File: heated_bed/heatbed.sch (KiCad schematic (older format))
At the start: 9 parts, among them P1 CONN_POWER, P2 CONN_2

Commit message: Feita a primeira metade da PCB, com duas trilhas de aquecimento prontas. Restam as duas trilhas com menos interferencia externa
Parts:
- removed P1: CONN_POWER, symbol CONN_2
- removed P2: CONN_2, symbol CONN_2
- added MH1, MH2, MH3, MH4: MOUNTING_HOLE, MountingHole_3mm_RevA_Date21Jun2010, symbol MOUNTING_HOLE
- added P1: CONN_4, bornier4, symbol CONN_4
- added PCB_R11, PCB_R21, PCB_R31, PCB_R41: 4R, SM1206, symbol R
- added TH2: 100k, SM0603, symbol THERMISTOR
- D1: footprint (none) -> LED-0805
- PCB_R1, PCB_R2, PCB_R3, PCB_R4: footprint (none) -> SM1206
- R1: footprint (none) -> SM0805
- TH1: footprint 0805,0603 -> SM0805
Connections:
- net labels added: Heater 1
- wire segments 16 -> 18
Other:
- moved on the sheet: PCB_R1, PCB_R2, PCB_R3, PCB_R4, R1, TH1

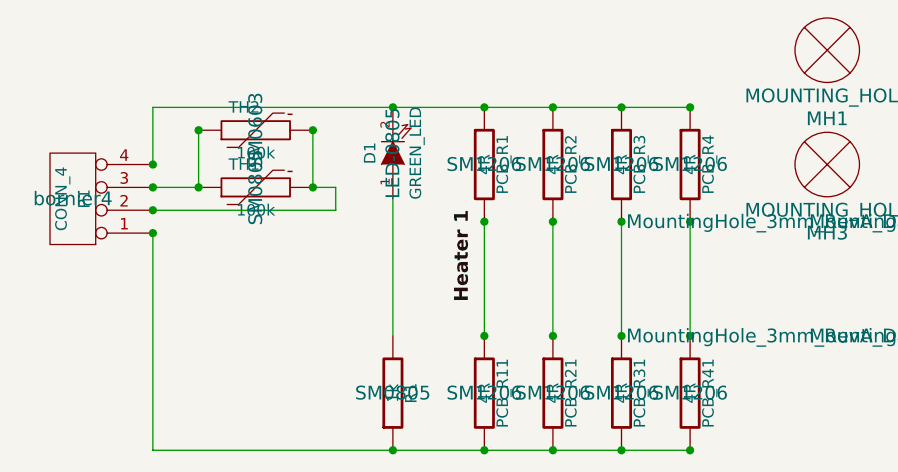
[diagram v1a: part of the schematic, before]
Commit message: Removidos resistores de PCB do esquematico para facilitar DRC.
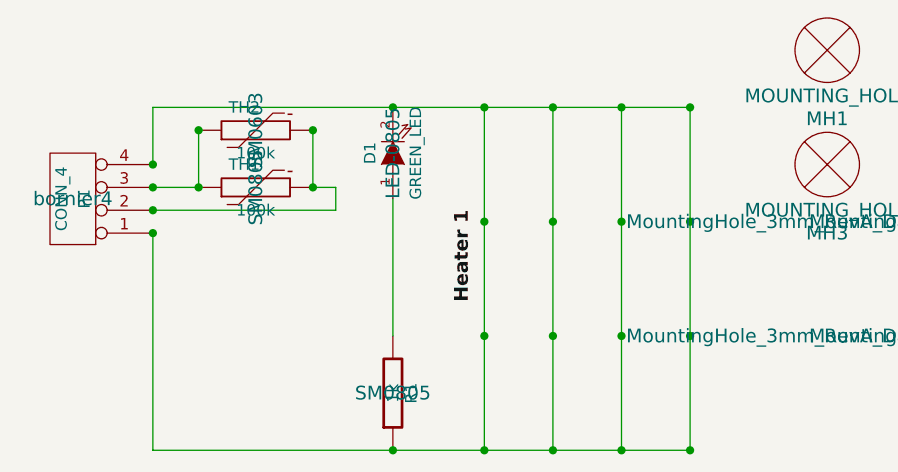
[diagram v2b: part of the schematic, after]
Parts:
- removed PCB_R1, PCB_R11, PCB_R2, PCB_R21, PCB_R3, PCB_R31, PCB_R4, PCB_R41: 4R, SM1206, symbol R
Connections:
- net at D1.2 (K), P1.4 (P4): now also P1.1 (P1), R1.1
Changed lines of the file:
@@
-EESchema Schematic File Version 2  date Sun 03 Mar 2013 11:04:40 PM BRT
+EESchema Schematic File Version 2  date Mon 04 Mar 2013 01:05:29 AM BRT
 LIBS:power
 LIBS:device
@@
 $EndComp
 $Comp
+L THERMISTOR TH1
+U 1 1 512596CC
+P 3250 5150
+F 0 "TH1" V 3350 5200 50  0000 C CNN
+F 1 "100k" V 3150 5150 50  0000 C CNN
+F 2 "SM0805" H 3250 5150 60  0000 C CNN
+F 3 "" H 3250 5150 60  0000 C CNN
+	1    3250 5150
+	0    -1   -1   0
+$EndComp
+$Comp
+L MOUNTING_HOLE MH1
+U 1 1 5133CB70
+P 5750 4550
+F 0 "MH1" H 5750 4250 60  0000 C CNN
+F 1 "MOUNTING_HOLE" H 5750 4350 60  0000 C CNN
+F 2 "MountingHole_3mm_RevA_Date21Jun2010" H 5750 3800 60  0000 C CNN
+F 3 "~" H 5750 3800 60  0000 C CNN
+	1    5750 4550
+	1    0    0    -1
+$EndComp
+$Comp
+L MOUNTING_HOLE MH2
+U 1 1 5133CB7D
+P 6550 4550
+F 0 "MH2" H 6550 4250 60  0000 C CNN
+F 1 "MOUNTING_HOLE" H 6550 4350 60  0000 C CNN
+F 2 "MountingHole_3mm_RevA_Date21Jun2010" H 6550 3800 60  0000 C CNN
+F 3 "~" H 6550 3800 60  0000 C CNN
+	1    6550 4550
+	1    0    0    -1
+$EndComp
+$Comp
+L MOUNTING_HOLE MH4
+U 1 1 5133CB83
+P 6550 5050
+F 0 "MH4" H 6550 4750 60  0000 C CNN
+F 1 "MOUNTING_HOLE" H 6550 4850 60  0000 C CNN
+F 2 "MountingHole_3mm_RevA_Date21Jun2010" H 6550 4300 60  0000 C CNN
+F 3 "~" H 6550 4300 60  0000 C CNN
+	1    6550 5050
+	1    0    0    -1
+$EndComp
+$Comp
+L MOUNTING_HOLE MH3
+U 1 1 5133CB89
+P 5750 5050
+F 0 "MH3" H 5750 4750 60  0000 C CNN
+F 1 "MOUNTING_HOLE" H 5750 4850 60  0000 C CNN
+F 2 "MountingHole_3mm_RevA_Date21Jun2010" H 5750 4300 60  0000 C CNN
+F 3 "~" H 5750 4300 60  0000 C CNN
+	1    5750 5050
+	1    0    0    -1
+$EndComp
+$Comp
+L CONN_4 P1
+U 1 1 5133D6B0
+P 2450 5200
+F 0 "P1" V 2400 5200 50  0000 C CNN
+F 1 "CONN_4" V 2500 5200 50  0000 C CNN
+F 2 "bornier4" H 2450 5200 60  0000 C CNN
+F 3 "" H 2450 5200 60  0000 C CNN
+	1    2450 5200
+	-1   0    0    1
+$EndComp
+Text Label 4200 5650 1    60   ~ 12
+Heater 1
+$Comp
+L THERMISTOR TH2
+U 1 1 51340120
+P 3250 4900
+F 0 "TH2" V 3350 4950 50  0000 C CNN
+F 1 "100k" V 3150 4900 50  0000 C CNN
+F 2 "SM0603" H 3250 4900 60  0000 C CNN
+F 3 "" H 3250 4900 60  0000 C CNN
+	1    3250 4900
+	0    -1   -1   0
+$EndComp
+Wire Wire Line
+	5150 6300 2800 6300
+Wire Wire Line
+	2800 4800 5150 4800
+Connection ~ 3850 4800
+Wire Wire Line
+	5150 4800 5150 6300
+Connection ~ 3850 6300
+Connection ~ 4850 4800
+Wire Wire Line
+	4850 4800 4850 6300
+Wire Wire Line
+	4550 4800 4550 6300
+Wire Wire Line
+	4250 4800 4250 6300
+Connection ~ 4250 4800
+Connection ~ 4550 4800
+Connection ~ 4250 5300
+Connection ~ 4550 5300
+Connection ~ 4850 5300
+Connection ~ 5150 5300
+Connection ~ 5150 4800
+Wire Wire Line
+	2800 4800 2800 5050
+Wire Wire Line
+	2800 5350 2800 6300
+Wire Wire Line
+	2800 5150 3000 5150
+Wire Wire Line
+	3500 5150 3600 5150
+Wire Wire Line
+	3600 5150 3600 5250
+Wire Wire Line
+	3600 5250 2800 5250
+Connection ~ 2800 5050
+Connection ~ 2800 5150
+Connection ~ 2800 5250
+Connection ~ 2800 5350
+Wire Wire Line
+	3850 5800 3850 5200
+Connection ~ 4250 6300
+Connection ~ 4550 6300
+Connection ~ 4850 6300
+Connection ~ 5150 6300
+Connection ~ 4250 5800
+Connection ~ 4550 5800
+Connection ~ 4850 5800
+Connection ~ 5150 5800
+Wire Wire Line
+	3000 5150 3000 4900
+Wire Wire Line
+	3500 4900 3500 5150
+Connection ~ 3500 5150
+Connection ~ 3500 4900
+Connection ~ 3000 4900
+Connection ~ 3000 5150
+$Comp
 L R R1
 U 1 1 512592C5
@@
 	1    0    0    1
 $EndComp
-Wire Wire Line
-	2800 6300 5150 6300
-Wire Wire Line
-	2800 4800 5150 4800
-Connection ~ 3850 4800
-Wire Wire Line
-	5150 5300 5150 5800
-Connection ~ 3850 6300
-Wire Wire Line
-	4850 4800 4850 4800
-Connection ~ 4850 4800
-Wire Wire Line
-	4850 5300 4850 5800
-Wire Wire Line
-	4550 5300 4550 5800
-Wire Wire Line
-	4250 5300 4250 5800
-Wire Wire Line
-	4250 4800 4250 4800
-Connection ~ 4250 4800
-Wire Wire Line
-	4550 4800 4550 4800
-Connection ~ 4550 4800
-$Comp
-L R PCB_R2
-U 1 1 51259665
-P 4550 5050
-F 0 "PCB_R2" V 4630 5050 50  0000 C CNN
-F 1 "4R" V 4550 5050 50  0000 C CNN
-F 2 "SM1206" H 4550 5050 60  0000 C CNN
-F 3 "" H 4550 5050 60  0000 C CNN
-	1    4550 5050
-	1    0    0    -1
-$EndComp
-$Comp
-L R PCB_R3
-U 1 1 5125966B
-P 4850 5050
-F 0 "PCB_R3" V 4930 5050 50  0000 C CNN
-F 1 "4R" V 4850 5050 50  0000 C CNN
-F 2 "SM1206" H 4850 5050 60  0000 C CNN
-F 3 "" H 4850 5050 60  0000 C CNN
-	1    4850 5050
-	1    0    0    -1
-$EndComp
-$Comp
-L R PCB_R4
-U 1 1 51259671
-P 5150 5050
-F 0 "PCB_R4" V 5230 5050 50  0000 C CNN
-F 1 "4R" V 5150 5050 50  0000 C CNN
-F 2 "SM1206" H 5150 5050 60  0000 C CNN
-F 3 "" H 5150 5050 60  0000 C CNN
-	1    5150 5050
-	1    0    0    -1
-$EndComp
-Connection ~ 4250 5300
-Connection ~ 4550 5300
-Connection ~ 4850 5300
-Connection ~ 5150 5300
-Connection ~ 5150 4800
-$Comp
-L THERMISTOR TH1
-U 1 1 512596CC
-P 3250 5150
-F 0 "TH1" V 3350 5200 50  0000 C CNN
-F 1 "100k" V 3150 5150 50  0000 C CNN
-F 2 "SM0805" H 3250 5150 60  0000 C CNN
-F 3 "" H 3250 5150 60  0000 C CNN
-	1    3250 5150
-	0    -1   -1   0
-$EndComp
-Wire Wire Line
-	2800 4800 2800 5050
-Wire Wire Line
-	2800 5350 2800 6300
-Wire Wire Line
-	2800 5150 3000 5150
-Wire Wire Line
-	3500 5150 3600 5150
-Wire Wire Line
-	3600 5150 3600 5250
-Wire Wire Line
-	3600 5250 2800 5250
-$Comp
-L MOUNTING_HOLE MH1
-U 1 1 5133CB70
-P 5750 4550
-F 0 "MH1" H 5750 4250 60  0000 C CNN
-F 1 "MOUNTING_HOLE" H 5750 4350 60  0000 C CNN
-F 2 "MountingHole_3mm_RevA_Date21Jun2010" H 5750 3800 60  0000 C CNN
-F 3 "~" H 5750 3800 60  0000 C CNN
-	1    5750 4550
-	1    0    0    -1
-$EndComp
-$Comp
-L MOUNTING_HOLE MH2
-U 1 1 5133CB7D
-P 6550 4550
-F 0 "MH2" H 6550 4250 60  0000 C CNN
-F 1 "MOUNTING_HOLE" H 6550 4350 60  0000 C CNN
-F 2 "MountingHole_3mm_RevA_Date21Jun2010" H 6550 3800 60  0000 C CNN
-F 3 "~" H 6550 3800 60  0000 C CNN
-	1    6550 4550
-	1    0    0    -1
-$EndComp
-$Comp
-L MOUNTING_HOLE MH4
-U 1 1 5133CB83
-P 6550 5050
-F 0 "MH4" H 6550 4750 60  0000 C CNN
-F 1 "MOUNTING_HOLE" H 6550 4850 60  0000 C CNN
-F 2 "MountingHole_3mm_RevA_Date21Jun2010" H 6550 4300 60  0000 C CNN
-F 3 "~" H 6550 4300 60  0000 C CNN
-	1    6550 5050
-	1    0    0    -1
-$EndComp
-$Comp
-L MOUNTING_HOLE MH3
-U 1 1 5133CB89
-P 5750 5050
-F 0 "MH3" H 5750 4750 60  0000 C CNN
-F 1 "MOUNTING_HOLE" H 5750 4850 60  0000 C CNN
-F 2 "MountingHole_3mm_RevA_Date21Jun2010" H 5750 4300 60  0000 C CNN
-F 3 "~" H 5750 4300 60  0000 C CNN
-	1    5750 5050
-	1    0    0    -1
-$EndComp
-$Comp
-L CONN_4 P1
-U 1 1 5133D6B0
-P 2450 5200
-F 0 "P1" V 2400 5200 50  0000 C CNN
-F 1 "CONN_4" V 2500 5200 50  0000 C CNN
-F 2 "bornier4" H 2450 5200 60  0000 C CNN
-F 3 "" H 2450 5200 60  0000 C CNN
-	1    2450 5200
-	-1   0    0    1
-$EndComp
-Connection ~ 2800 5050
-Connection ~ 2800 5150
-Connection ~ 2800 5250
-Connection ~ 2800 5350
-Wire Wire Line
-	3850 5800 3850 5200
-$Comp
-L R PCB_R41
-U 1 1 5133E699
-P 5150 6050
-F 0 "PCB_R41" V 5230 6050 50  0000 C CNN
-F 1 "4R" V 5150 6050 50  0000 C CNN
-F 2 "SM1206" H 5150 6050 60  0000 C CNN
-F 3 "" H 5150 6050 60  0000 C CNN
-	1    5150 6050
-	1    0    0    -1
-$EndComp
-Connection ~ 4250 6300
-Connection ~ 4550 6300
-Connection ~ 4850 6300
-Connection ~ 5150 6300
-Connection ~ 4250 5800
-Connection ~ 4550 5800
-Connection ~ 4850 5800
-Connection ~ 5150 5800
-Text Label 4200 5650 1    60   ~ 12
-Heater 1
-$Comp
-L R PCB_R31
-U 1 1 5133E693
-P 4850 6050
-F 0 "PCB_R31" V 4930 6050 50  0000 C CNN
-F 1 "4R" V 4850 6050 50  0000 C CNN
-F 2 "SM1206" H 4850 6050 60  0000 C CNN
-F 3 "" H 4850 6050 60  0000 C CNN
-	1    4850 6050
-	1    0    0    -1
-$EndComp
-$Comp
-L R PCB_R21
-U 1 1 5133E68D
-P 4550 6050
-F 0 "PCB_R21" V 4630 6050 50  0000 C CNN
-F 1 "4R" V 4550 6050 50  0000 C CNN
-F 2 "SM1206" H 4550 6050 60  0000 C CNN
-F 3 "" H 4550 6050 60  0000 C CNN
-	1    4550 6050
-	1    0    0    -1
-$EndComp
-$Comp
-L R PCB_R11
-U 1 1 5133E614
-P 4250 6050
-F 0 "PCB_R11" V 4330 6050 50  0000 C CNN
-F 1 "4R" V 4250 6050 50  0000 C CNN
-F 2 "SM1206" H 4250 6050 60  0000 C CNN
-F 3 "" H 4250 6050 60  0000 C CNN
-	1    4250 6050
-	1    0    0    -1
-$EndComp
-$Comp
-L R PCB_R1
-U 1 1 5125956A
-P 4250 5050
-F 0 "PCB_R1" V 4330 5050 50  0000 C CNN
-F 1 "4R" V 4250 5050 50  0000 C CNN
-F 2 "SM1206" H 4250 5050 60  0000 C CNN
-F 3 "" H 4250 5050 60  0000 C CNN
-	1    4250 5050
-	1    0    0    -1
-$EndComp
-$Comp
-L THERMISTOR TH2
-U 1 1 51340120
-P 3250 4900
-F 0 "TH2" V 3350 4950 50  0000 C CNN
-F 1 "100k" V 3150 4900 50  0000 C CNN
-F 2 "SM0603" H 3250 4900 60  0000 C CNN
-F 3 "" H 3250 4900 60  0000 C CNN
-	1    3250 4900
-	0    -1   -1   0
-$EndComp
-Wire Wire Line
-	3000 5150 3000 4900
-Wire Wire Line
-	3500 4900 3500 5150
-Connection ~ 3500 5150
-Connection ~ 3500 4900
-Connection ~ 3000 4900
-Connection ~ 3000 5150
 $EndSCHEMATC

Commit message: Placa assinada
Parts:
- added N1: AYLONS, ~, symbol AYLONS
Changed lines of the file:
@@
-EESchema Schematic File Version 2  date Mon 04 Mar 2013 01:05:29 AM BRT
+EESchema Schematic File Version 2  date Wed 06 Mar 2013 12:02:39 AM BRT
 LIBS:power
 LIBS:device
@@
 Sheet 1 1
 Title "Heat Bed for Metamáquina 2"
-Date "4 mar 2013"
+Date "6 mar 2013"
 Rev "0.9"
 Comp "Gustavo Barbosa Monteiro Bruno for Metamáquina"
@@
 	2800 4800 2800 5050
 Wire Wire Line
-	2800 5350 2800 6300
+	2800 6300 2800 5350
 Wire Wire Line
 	2800 5150 3000 5150
@@
 	1    0    0    1
 $EndComp
+$Comp
+L AYLONS N1
+U 1 1 5136AF98
+P 11000 7000
+F 0 "N1" H 10700 7550 60  0000 C CNN
+F 1 "AYLONS" H 10700 7400 60  0000 C CNN
+F 2 "~" H 10900 7100 60  0000 C CNN
+F 3 "~" H 10900 7100 60  0000 C CNN
+	1    11000 7000
+	1    0    0    -1
+$EndComp
 $EndSCHEMATC
